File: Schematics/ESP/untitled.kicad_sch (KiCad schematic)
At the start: 5 parts, among them J1 Conn_01x04_Male, J2 Conn_01x04_Male, U1 NUCLEO64-F411RE

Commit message: Schematics
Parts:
- R1, R2: footprint (none) -> Resistor_SMD:R_1206_3216Metric_Pad1.30x1.75mm_HandSolder
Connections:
- net Regulated 5V is gone; now on net +5V: U1.6 (E5V)
- net Battery level: now reaches U1.30 (PA1)
- net Signal renamed Fan Signal
- no-connect marks 50 -> 51
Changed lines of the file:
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@@
   (no_connect (at 165.1 93.98))
   (no_connect (at 127 45.72))
+  (no_connect (at 132.08 45.72))
   (no_connect (at 165.1 111.76))
   (no_connect (at 165.1 91.44))
@@
     (effects (font (size 1.27 1.27)) (justify left bottom))
   )
-  (global_label "Signal" (shape output) (at 173.99 116.84 0) (fields_autoplaced)
+  (global_label "Fan Signal" (shape output) (at 173.99 116.84 0) (fields_autoplaced)
     (effects (font (size 1.27 1.27)) (justify left))
-    (property "Intersheetrefs" "${INTERSHEET_REFS}" (at 182.3298 116.7606 0)
+    (property "Intersheetrefs" "${INTERSHEET_REFS}" (at 186.9709 116.84 0)
       (effects (font (size 1.27 1.27)) (justify left) hide)
     )
@@
     )
   )
-  (global_label "Regulated 5V" (shape input) (at 124.46 38.1 90) (fields_autoplaced)
+  (global_label "+5V" (shape input) (at 124.46 38.1 90) (fields_autoplaced)
     (effects (font (size 1.27 1.27)) (justify left))
-    (property "Intersheetrefs" "${INTERSHEET_REFS}" (at 124.46 22.7 90)
+    (property "Intersheetrefs" "${INTERSHEET_REFS}" (at 124.46 31.3237 90)
       (effects (font (size 1.27 1.27)) (justify left) hide)
     )
@@
     )
   )
+  (global_label "Battery level" (shape input) (at 177.8 60.96 0) (fields_autoplaced)
+    (effects (font (size 1.27 1.27)) (justify left))
+    (property "Intersheetrefs" "${INTERSHEET_REFS}" (at 192.6558 60.96 0)
+      (effects (font (size 1.27 1.27)) (justify left) hide)
+    )
+  )
   (global_label "Motion Sensor A" (shape input) (at 100.33 104.14 180) (fields_autoplaced)
     (effects (font (size 1.27 1.27)) (justify right))
@@
       (effects (font (size 1.27 1.27)) (justify left))
     )
-    (property "Footprint" "" (at 196.342 129.54 90)
+    (property "Footprint" "Resistor_SMD:R_1206_3216Metric_Pad1.30x1.75mm_HandSolder" (at 196.342 129.54 90)
       (effects (font (size 1.27 1.27)) hide)
     )
@@
       (effects (font (size 1.27 1.27)) (justify left))
     )
-    (property "Footprint" "" (at 187.452 129.54 90)
-      (effects (font (size 1.27 1.27)) hide)
-    )
+    (property "Footprint" "Resistor_SMD:R_1206_3216Metric_Pad1.30x1.75mm_HandSolder" (at 187.452 129.54 90)
+      (effects (font (size 1.27 1.27)) hide)
+    )

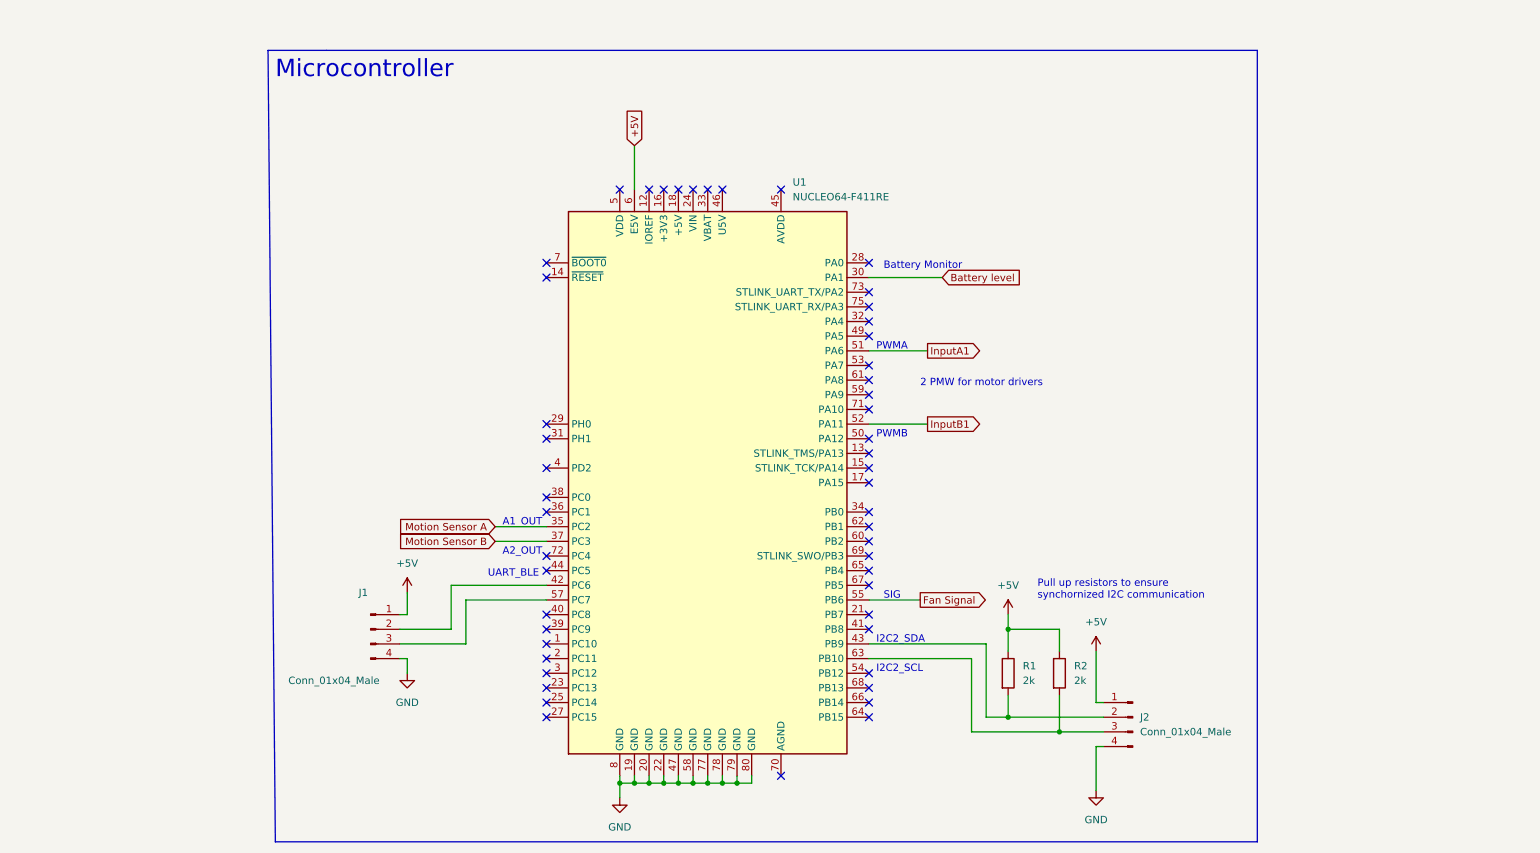
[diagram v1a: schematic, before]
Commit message: Added footprints, IR pins and bill of materials-Khalil
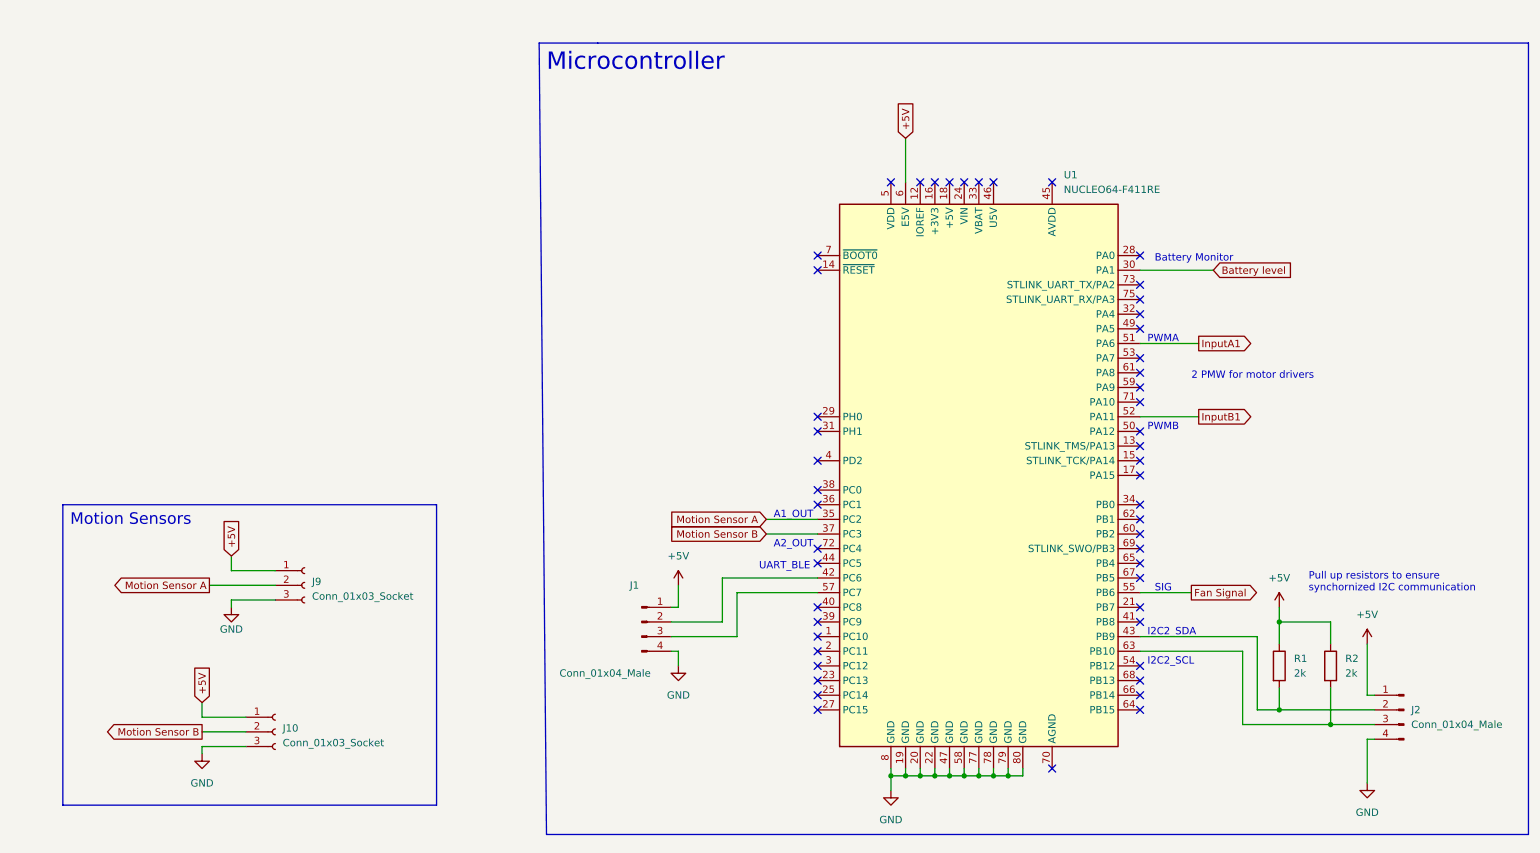
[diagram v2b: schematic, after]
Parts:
- added J10, J9: Conn_01x03_Socket, Connector_PinHeader_1.00mm:PinHeader_1x03_P1.00mm_Vertical, symbol Connector:Conn_01x03_Socket
- J1, J2: footprint (none) -> Connector_PinSocket_1.00mm:PinSocket_1x04_P1.00mm_Vertical
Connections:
- net +5V: now also J10.1 (Pin_1), J9.1 (Pin_1)
- net GND: now also J10.3 (Pin_3), J9.3 (Pin_3)
- net Motion Sensor A: now also J9.2 (Pin_2)
- net Motion Sensor B: now also J10.2 (Pin_2)
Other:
- note added: "Motion Sensors"
- moved on the sheet: J1, J2, R1, R2, U1

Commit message: newer BOM
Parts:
- J1, J2: Price (none) -> 1,29; digikey link (none) -> https://www.digikey.fi/fi/products/detail/kyocera-avx/00927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
- J10, J9: Price (none) -> 0,68; digikey link (none) -> https://www.digikey.it/en/products/detail/metz-connect-usa-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
- R1, R2: Price (none) -> 0,46; digikey link (none) -> https://www.digikey.fi/en/products/detail/yageo/RT0402BRD07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
- U1: Price (none) -> 0; digikey link (none) -> Gotten from class
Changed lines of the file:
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@@
+      (effects (font (size 1.27 1.27)) hide)
+    )
+    (property "digikey link" "https://www.digikey.fi/en/products/detail/yageo/RT0402BRD072KL/1069198" (at 245.11 128.27 0)
+      (effects (font (size 1.27 1.27)) hide)
+    )
+    (property "Price" "0,46" (at 245.11 128.27 0)
       (effects (font (size 1.27 1.27)) hide)
     )
@@
       (effects (font (size 1.27 1.27)) hide)
     )
+    (property "digikey link" "https://www.digikey.fi/fi/products/detail/kyocera-avx/009276004021106/2346141" (at 125.73 120.65 0)
+      (effects (font (size 1.27 1.27)) hide)
+    )
+    (property "Price" "1,29" (at 125.73 120.65 0)
+      (effects (font (size 1.27 1.27)) hide)
+    )
     (pin "1")
     (pin "2")
@@
       (effects (font (size 1.27 1.27)) hide)
     )
+    (property "digikey link" "https://www.digikey.fi/fi/products/detail/kyocera-avx/009276004021106/2346141" (at 257.81 135.89 0)
+      (effects (font (size 1.27 1.27)) hide)
+    )
+    (property "Price" "1,29" (at 257.81 135.89 0)
+      (effects (font (size 1.27 1.27)) hide)
+    )
     (pin "1")
     (pin "2")
@@
     )
     (property "Datasheet" "http://www.st.com/st-web-ui/static/active/en/resource/technical/document/data_brief/DM00105918.pdf" (at 161.29 130.81 0)
+      (effects (font (size 1.27 1.27)) hide)
+    )
+    (property "digikey link" "Gotten from class" (at 184.15 95.25 0)
+      (effects (font (size 1.27 1.27)) hide)
+    )
+    (property "Price" "0" (at 184.15 95.25 0)
       (effects (font (size 1.27 1.27)) hide)
     )
@@
       (effects (font (size 1.27 1.27)) hide)
     )
+    (property "digikey link" "https://www.digikey.fi/en/products/detail/yageo/RT0402BRD072KL/1069198" (at 236.22 128.27 0)
+      (effects (font (size 1.27 1.27)) hide)
+    )
+    (property "Price" "0,46" (at 236.22 128.27 0)
+      (effects (font (size 1.27 1.27)) hide)
+    )
     (pin "1")
     (pin "2")
@@
     )
     (property "Datasheet" "~" (at 62.23 139.7 0)
+      (effects (font (size 1.27 1.27)) hide)
+    )
+    (property "digikey link" "https://www.digikey.it/en/products/detail/metz-connect-usa-inc/31017103/7794879" (at 62.23 139.7 0)
+      (effects (font (size 1.27 1.27)) hide)
+    )
+    (property "Price" "0,68" (at 62.23 139.7 0)
       (effects (font (size 1.27 1.27)) hide)
     )
@@
       (effects (font (size 1.27 1.27)) hide)
     )
+    (property "digikey link" "https://www.digikey.it/en/products/detail/metz-connect-usa-inc/31017103/7794879" (at 67.31 114.3 0)
+      (effects (font (size 1.27 1.27)) hide)
+    )
+    (property "Price" "0,68" (at 67.31 114.3 0)
+      (effects (font (size 1.27 1.27)) hide)
+    )
